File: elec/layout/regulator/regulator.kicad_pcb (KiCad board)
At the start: 2 copper layers, 13 parts, among them U1 _Texas_Instruments_TPS56637RP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

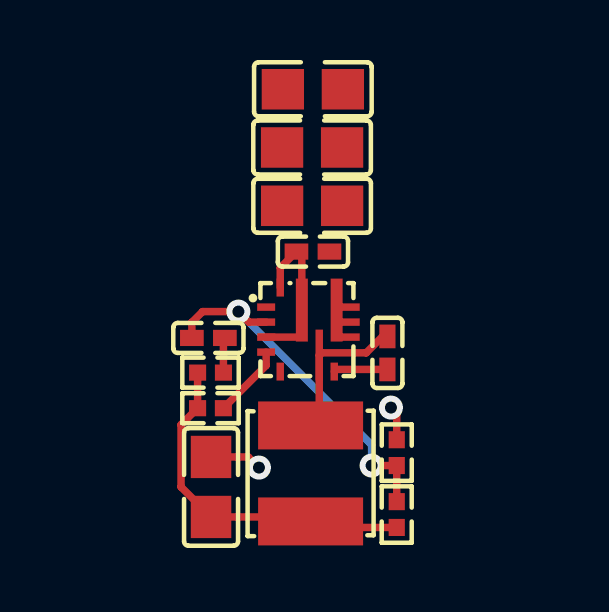
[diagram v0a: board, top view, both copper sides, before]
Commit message: delete unused modules and add library parts
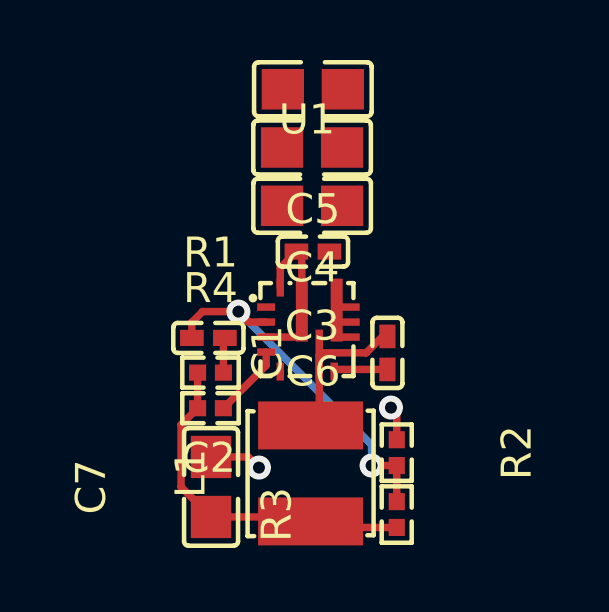
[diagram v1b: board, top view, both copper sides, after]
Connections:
- C1 pad 1: net -> net-5
- C1 pad 2: net-1 -> net-6
- C2 pad 1: net-2 -> net-1
- C2 pad 2: net-3 -> net-4
- C3 pad 1: net-4 -> net-2
- C3 pad 2: net-5 -> net-3
- C4 pad 1: net-4 -> net-2
- C4 pad 2: net-5 -> net-3
- C5 pad 1: net-4 -> net-2
- C5 pad 2: net-5 -> net-3
- C6 pad 1: net-4 -> net-2
- C6 pad 2: net-5 -> net-3
- C7 pad 1: net-6 -> net
- C7 pad 2: net-5 -> net-3
- L1 pad 1: net-6 -> net
- L1 pad 2: net-1 -> net-6
- R1 pad 1: net-6 -> net
- R1 pad 2: net-2 -> net-1
- R2 pad 1: net-5 -> net-3
- R2 pad 2: net-3 -> net-4
- R3 pad 1: net-6 -> net
- R3 pad 2: net-3 -> net-4
- R4 pad 1: net-6 -> net
- U1 pad 10: net-5 -> net-3
- U1 pad 2: net-3 -> net-4
- U1 pad 3: net-5 -> net-3
- U1 pad 6: net-1 -> net-6
- U1 pad 7: net -> net-5
- U1 pad 8: net-4 -> net-2
- U1 pad 9: net-5 -> net-3

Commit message: cleanup unused files + standardize naming
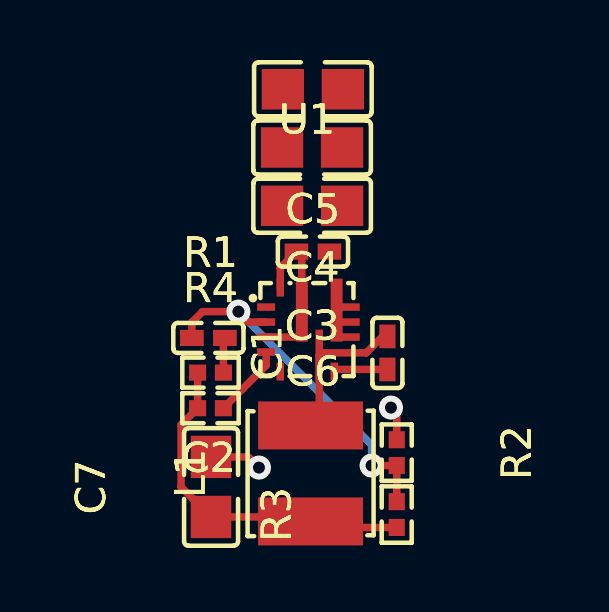
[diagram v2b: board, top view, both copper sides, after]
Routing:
- net net-4: track 0.00 -> 12.3 mm, vias 0 -> 2
- net net: track 1.80 -> 11.8 mm
- net net-6: track 11.8 -> 4.99 mm
- net net-5: track 8.40 -> 1.80 mm, vias 2 -> 0
- net net-3: track 12.3 -> 8.40 mm
- net net-1: track 4.99 -> 1.18 mm
- net net-2: track 1.18 -> 0.00 mm

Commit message: import copper features to hat board
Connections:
- C1 pad 1: net-5 -> net-6
- C1 pad 2: net-6 -> net-5
- C2 pad 2: net-4 -> net-3
- C3 pad 1: net-2 -> net-4
- C3 pad 2: net-3 -> net-2
- C4 pad 1: net-2 -> net-4
- C4 pad 2: net-3 -> net-2
- C5 pad 1: net-2 -> net-4
- C5 pad 2: net-3 -> net-2
- C6 pad 1: net-2 -> net-4
- C6 pad 2: net-3 -> net-2
- C7 pad 2: net-3 -> net-2
- L1 pad 2: net-6 -> net-5
- R2 pad 1: net-3 -> net-2
- R2 pad 2: net-4 -> net-3
- R3 pad 2: net-4 -> net-3
- U1 pad 10: net-3 -> net-2
- U1 pad 2: net-4 -> net-3
- U1 pad 3: net-3 -> net-2
- U1 pad 6: net-6 -> net-5
- U1 pad 7: net-5 -> net-6
- U1 pad 8: net-2 -> net-4
- U1 pad 9: net-3 -> net-2

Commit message: builds working
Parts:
- C1: value (none) -> 100nF ±10% 16V X7R
- C4, C5: value (none) -> 4.7µF ±10% 25V X5R
- R1: value 20kΩ ±1% 62.5mW -> 22kΩ ±1% 62.5mW
- R2: value 10kΩ ±1% 62.5mW -> 8.2kΩ ±1% 62.5mW
- R3: value 75kΩ ±5% 62.5mW -> 68kΩ ±1% 62.5mW
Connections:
- C1 pad 1: net-6 -> net-7
- C1 pad 2: net-5 -> net-6
- C2 pad 1: net-1 -> net-4
- C2 pad 2: net-3 -> net-5
- C3 pad 1: net-4 -> net
- C3 pad 2: net-2 -> net-1
- C4 pad 1: net-4 -> net
- C4 pad 2: net-2 -> net-1
- C5 pad 1: net-4 -> net
- C5 pad 2: net-2 -> net-1
- C6 pad 1: net-4 -> net
- C6 pad 2: net-2 -> net-1
- C7 pad 1: net -> net-2
- C7 pad 2: net-2 -> net-1
- L1 pad 1: net -> net-2
- L1 pad 2: net-5 -> net-6
- R1 pad 1: net -> net-2
- R1 pad 2: net-1 -> net-4
- R2 pad 1: net-2 -> net-1
- R2 pad 2: net-3 -> net-5
- R3 pad 1: net -> net-2
- R3 pad 2: net-3 -> net-5
- R4 pad 1: net -> net-2
- R4 pad 2: net-7 -> net-3
- U1 pad 10: net-2 -> net-1
- U1 pad 2: net-3 -> net-5
- U1 pad 3: net-2 -> net-1
- U1 pad 4: net-7 -> net-3
- U1 pad 6: net-5 -> net-6
- U1 pad 7: net-6 -> net-7
- U1 pad 8: net-4 -> net
- U1 pad 9: net-2 -> net-1
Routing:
- net net-4: track 12.3 -> 0.00 mm, vias 2 -> 0
- net net-2: track 0.00 -> 8.40 mm, vias 0 -> 2
- net net-3: track 8.40 -> 12.3 mm
- net net-6: track 4.99 -> 1.80 mm
- net net-5: track 1.80 -> 4.99 mm

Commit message: Update PCB version to kicad9; Disable non-existing builds
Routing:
- net net: track 11.8 -> 0.00 mm
- net net-3: track 12.3 -> 2.46 mm, vias 2 -> 0
- net net-5: track 4.99 -> 12.3 mm, vias 0 -> 2
- net net-1: track 1.18 -> 8.40 mm, vias 0 -> 2
- net net-2: track 8.40 -> 11.8 mm, vias 2 -> 0
- net net-6: track 1.80 -> 4.99 mm
- net net-4: track 0.00 -> 1.18 mm
- net net-7: track 2.46 -> 1.80 mm
